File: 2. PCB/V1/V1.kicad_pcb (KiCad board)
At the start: 2 copper layers, 80 x 65 mm, 37 parts, among them J1 LCD I2C, J2 USB_C_Receptacle_USB2.0_16P, J4 Conn_01x05_Socket, Q1 S8550, SW1 RESET, SW2 SW_Push, SW3 SW_Push, SW4 SW_Push, SW5 SW_Push, SW6 SW_Push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

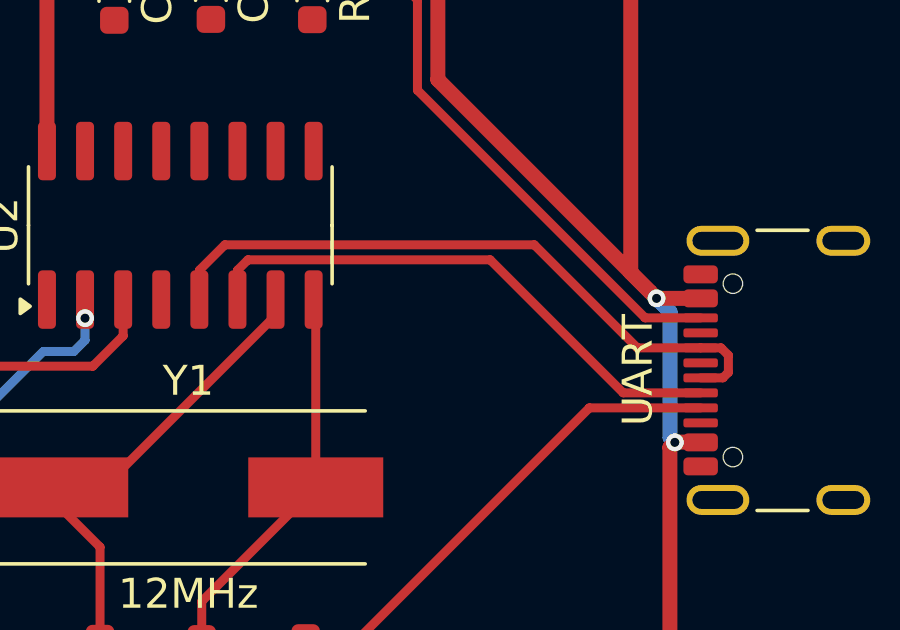
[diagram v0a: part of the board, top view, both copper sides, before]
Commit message: completed pcd and lcd_i2c lib
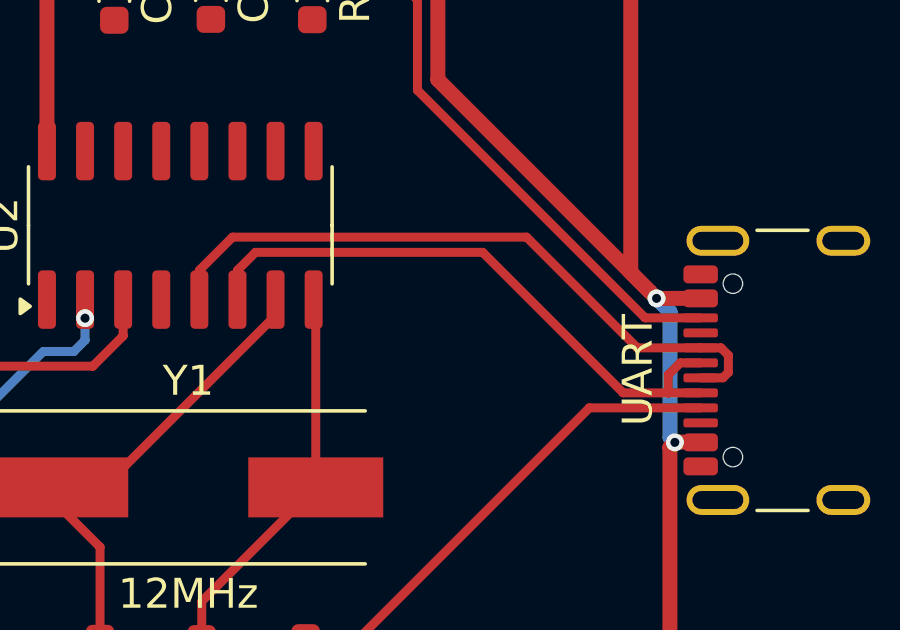
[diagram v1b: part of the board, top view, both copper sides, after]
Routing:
- net /D-: track 18.4 -> 20.4 mm
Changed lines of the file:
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@@
 	)
 	(segment
-		(start 175.875 97.285)
-		(end 179.31 100.72)
+		(start 164.71 98.135001)
+		(end 165.817001 97.028)
 		(width 0.3)
 		(layer "F.Cu")
@@
 	)
 	(segment
-		(start 179.31 100.72)
-		(end 181.42 100.72)
-		(width 0.3)
-		(layer "F.Cu")
-		(net 5)
-	)
-	(segment
 		(start 182.345 101.535)
 		(end 182.16 101.72)
-		(width 0.3)
-		(layer "F.Cu")
-		(net 5)
-	)
-	(segment
-		(start 165.560001 97.285)
-		(end 175.875 97.285)
 		(width 0.3)
 		(layer "F.Cu")
@@
 	)
 	(segment
+		(start 175.618 97.028)
+		(end 179.31 100.72)
+		(width 0.3)
+		(layer "F.Cu")
+		(net 5)
+	)
+	(segment
+		(start 165.817001 97.028)
+		(end 175.618 97.028)
+		(width 0.3)
+		(layer "F.Cu")
+		(net 5)
+	)
+	(segment
 		(start 182.345 100.96688)
 		(end 182.345 101.535)
@@
 	)
 	(segment
-		(start 164.71 98.135001)
-		(end 165.560001 97.285)
+		(start 179.31 100.72)
+		(end 181.42 100.72)
 		(width 0.3)
 		(layer "F.Cu")
@@
 	)
 	(segment
-		(start 165.98 98.135001)
-		(end 166.330001 97.785)
+		(start 178.84 102.22)
+		(end 180.34 102.22)
 		(width 0.3)
 		(layer "F.Cu")
@@
 	)
 	(segment
-		(start 166.330001 97.785)
-		(end 174.405 97.785)
+		(start 165.98 98.135001)
+		(end 166.579001 97.536)
+		(width 0.3)
+		(layer "F.Cu")
+		(net 7)
+	)
+	(segment
+		(start 166.579001 97.536)
+		(end 174.156 97.536)
+		(width 0.3)
+		(layer "F.Cu")
+		(net 7)
+	)
+	(segment
+		(start 180.34 102.22)
+		(end 181.42 102.22)
+		(width 0.3)
+		(layer "F.Cu")
+		(net 7)
+	)
+	(segment
+		(start 180.34 101.62188)
+		(end 180.34 102.22)
 		(width 0.3)
 		(layer "F.Cu")
@@
 	)
 	(segment
-		(start 178.84 102.22)
-		(end 181.42 102.22)
+		(start 180.74188 101.22)
+		(end 180.34 101.62188)
 		(width 0.3)
 		(layer "F.Cu")
@@
 	)
 	(segment
-		(start 174.405 97.785)
+		(start 181.42 101.22)
+		(end 180.74188 101.22)
+		(width 0.3)
+		(layer "F.Cu")
+		(net 7)
+	)
+	(segment
+		(start 174.156 97.536)
 		(end 178.84 102.22)
 		(width 0.3)
